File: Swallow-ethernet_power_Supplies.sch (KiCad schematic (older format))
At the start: 25 parts, among them P6 V_In, P7 +5V_In, U11 NCP1529, U12 NCP1529, U13 NCP303LSN09T1G

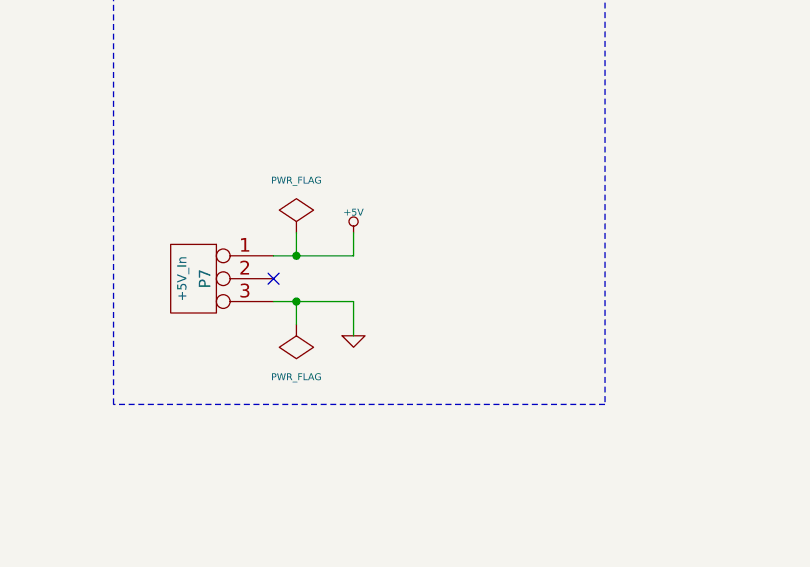
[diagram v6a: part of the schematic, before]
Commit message: Added another +5V header and cleaned up via inside PCIe header.
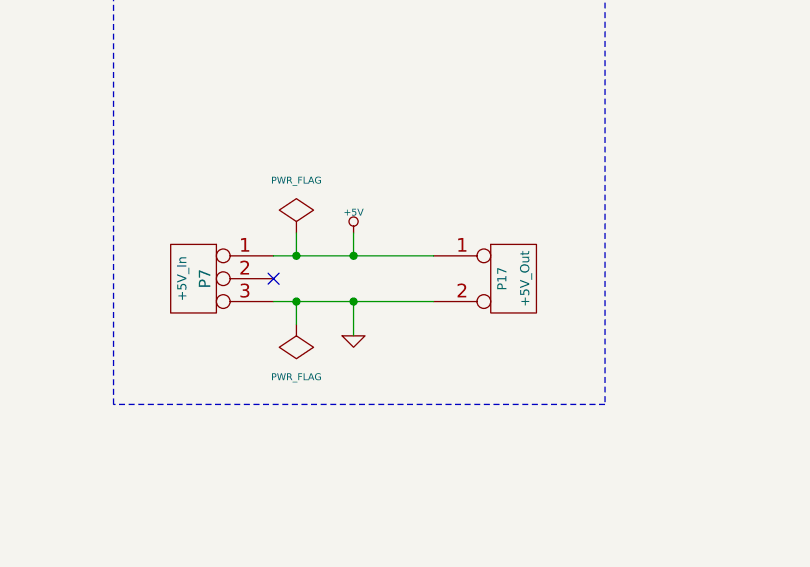
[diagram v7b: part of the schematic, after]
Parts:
- added P17: +5V_Out, symbol CONN_2
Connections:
- net +5V: now also P17.1 (P1)
- net GND: now also P17.2 (PM)
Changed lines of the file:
@@
-EESchema Schematic File Version 2  date Thu 11 Oct 2012 17:02:03 BST
+EESchema Schematic File Version 2  date Tue 16 Oct 2012 12:12:08 BST
 LIBS:power
 LIBS:device
@@
 Sheet 4 4
 Title ""
-Date "11 oct 2012"
+Date "16 oct 2012"
 Rev ""
 Comp ""
@@
 Comment4 ""
 $EndDescr
-Text Notes 7050 6650 0    60   ~ 0
-100nF should give >100us transitions
+Connection ~ 7900 2200
+Wire Wire Line
+	8250 2200 7550 2200
 Wire Wire Line
 	9700 6550 9700 5850
@@
 Connection ~ 7650 2000
 Wire Wire Line
-	7900 2350 7900 2200
+	7900 2200 7900 2350
 Wire Wire Line
 	5800 5400 4700 5400
@@
 Connection ~ 1950 5400
 Wire Wire Line
-	7900 1900 7900 2000
+	7900 2000 7900 1900
 Wire Notes Line
 	9000 850  6850 850
@@
 Connection ~ 9700 6100
 Wire Wire Line
-	7900 2000 7550 2000
-Wire Wire Line
 	2300 6000 2300 5800
 Wire Wire Line
@@
 Connection ~ 1850 5400
 Wire Wire Line
-	7900 2200 7550 2200
+	8250 2000 7550 2000
+Connection ~ 7900 2000
+$Comp
+L CONN_2 P17
+U 1 1 507D3FF4
+P 8600 2100
+F 0 "P17" V 8550 2100 40  0000 C CNN
+F 1 "+5V_Out" V 8650 2100 40  0000 C CNN
+	1    8600 2100
+	1    0    0    -1
+$EndComp
+Text Notes 7050 6650 0    60   ~ 0
+100nF should give >100us transitions
 NoConn ~ 7550 2100
 $Comp
@@
 $EndComp
 $Comp
-L +3.3V #PWR63
+L +3.3V #PWR062
 U 1 1 4F5FB6A5
 P 2300 5800
-F 0 "#PWR63" H 2300 5760 30  0001 C CNN
+F 0 "#PWR062" H 2300 5760 30  0001 C CNN
 F 1 "+3.3V" H 2300 5910 30  0000 C CNN
 	1    2300 5800
@@
 $EndComp
 $Comp
-L VDD #PWR67
+L VDD #PWR063
 U 1 1 4ED160AA
 P 5800 5400
-F 0 "#PWR67" H 5800 5500 30  0001 C CNN
+F 0 "#PWR063" H 5800 5500 30  0001 C CNN
 F 1 "VDD" H 5800 5510 30  0000 C CNN
 	1    5800 5400
@@
 NoConn ~ 9050 6150
 $Comp
-L GND #PWR68
+L GND #PWR064
 U 1 1 4EDA727F
 P 7350 6450
-F 0 "#PWR68" H 7350 6450 30  0001 C CNN
+F 0 "#PWR064" H 7350 6450 30  0001 C CNN
 F 1 "GND" H 7350 6380 30  0001 C CNN
 	1    7350 6450
@@
 $EndComp
 $Comp
-L VDD #PWR69
+L VDD #PWR065
 U 1 1 4EDA7272
 P 7400 5700
-F 0 "#PWR69" H 7400 5800 30  0001 C CNN
+F 0 "#PWR065" H 7400 5800 30  0001 C CNN
 F 1 "VDD" H 7400 5810 30  0000 C CNN
 	1    7400 5700
@@
 $EndComp
 $Comp
-L PWR_FLAG #FLG3
+L PWR_FLAG #FLG066
 U 1 1 4ED16457
 P 5650 5100
-F 0 "#FLG3" H 5650 5370 30  0001 C CNN
+F 0 "#FLG066" H 5650 5370 30  0001 C CNN
 F 1 "PWR_FLAG" H 5650 5330 30  0000 C CNN
 	1    5650 5100
@@
 $EndComp
 $Comp
-L PWR_FLAG #FLG2
+L PWR_FLAG #FLG067
 U 1 1 4ED16447
 P 5600 1700
-F 0 "#FLG2" H 5600 1970 30  0001 C CNN
+F 0 "#FLG067" H 5600 1970 30  0001 C CNN
 F 1 "PWR_FLAG" H 5600 1930 30  0000 C CNN
 	1    5600 1700
@@
 $EndComp
 $Comp
-L PWR_FLAG #FLG5
+L PWR_FLAG #FLG068
 U 1 1 4ED162B6
 P 7650 2300
-F 0 "#FLG5" H 7650 2570 30  0001 C CNN
+F 0 "#FLG068" H 7650 2570 30  0001 C CNN
 F 1 "PWR_FLAG" H 7650 2530 30  0000 C CNN
 	1    7650 2300
@@
 $EndComp
 $Comp
-L PWR_FLAG #FLG4
+L PWR_FLAG #FLG069
 U 1 1 4ED16176
 P 7650 1900
-F 0 "#FLG4" H 7650 2170 30  0001 C CNN
+F 0 "#FLG069" H 7650 2170 30  0001 C CNN
 F 1 "PWR_FLAG" H 7650 2130 30  0000 C CNN
 	1    7650 1900
@@
 $EndComp
 $Comp
-L +5V #PWR70
+L +5V #PWR070
 U 1 1 4ED1613C
 P 7900 1900
-F 0 "#PWR70" H 7900 1990 20  0001 C CNN
+F 0 "#PWR070" H 7900 1990 20  0001 C CNN
 F 1 "+5V" H 7900 1990 30  0000 C CNN
 	1    7900 1900
@@
 $EndComp
 $Comp
-L GND #PWR71
+L GND #PWR071
 U 1 1 4ED16138
 P 7900 2350
-F 0 "#PWR71" H 7900 2350 30  0001 C CNN
+F 0 "#PWR071" H 7900 2350 30  0001 C CNN
 F 1 "GND" H 7900 2280 30  0001 C CNN
 	1    7900 2350
@@
 $EndComp
 $Comp
-L GND #PWR65
+L GND #PWR072
 U 1 1 4ED16054
 P 3150 6600
-F 0 "#PWR65" H 3150 6600 30  0001 C CNN
+F 0 "#PWR072" H 3150 6600 30  0001 C CNN
 F 1 "GND" H 3150 6530 30  0001 C CNN
 	1    3150 6600
@@
 $EndComp
 $Comp
-L +5V #PWR62
+L +5V #PWR073
 U 1 1 4ED1604D
 P 1750 5400
-F 0 "#PWR62" H 1750 5490 20  0001 C CNN
+F 0 "#PWR073" H 1750 5490 20  0001 C CNN
 F 1 "+5V" H 1750 5490 30  0000 C CNN
 	1    1750 5400
@@
 5V to 3.3V at 1A Step-down
 $Comp
-L +5V #PWR61
+L +5V #PWR074
 U 1 1 4ED15FDA
 P 1750 2000
-F 0 "#PWR61" H 1750 2090 20  0001 C CNN
+F 0 "#PWR074" H 1750 2090 20  0001 C CNN
 F 1 "+5V" H 1750 2090 30  0000 C CNN
 	1    1750 2000
@@
 $EndComp
 $Comp
-L +3.3V #PWR66
+L +3.3V #PWR075
 U 1 1 4ED15FB8
 P 5700 2000
-F 0 "#PWR66" H 5700 1960 30  0001 C CNN
+F 0 "#PWR075" H 5700 1960 30  0001 C CNN
 F 1 "+3.3V" H 5700 2110 30  0000 C CNN
 	1    5700 2000
@@
 $EndComp
 $Comp
-L GND #PWR64
+L GND #PWR076
 U 1 1 4ED15EEA
 P 3150 3200
-F 0 "#PWR64" H 3150 3200 30  0001 C CNN
+F 0 "#PWR076" H 3150 3200 30  0001 C CNN
 F 1 "GND" H 3150 3130 30  0001 C CNN
 	1    3150 3200
